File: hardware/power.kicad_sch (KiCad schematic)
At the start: 12 parts, among them Q1 DMG2305UX, U3 TPS61099DRV

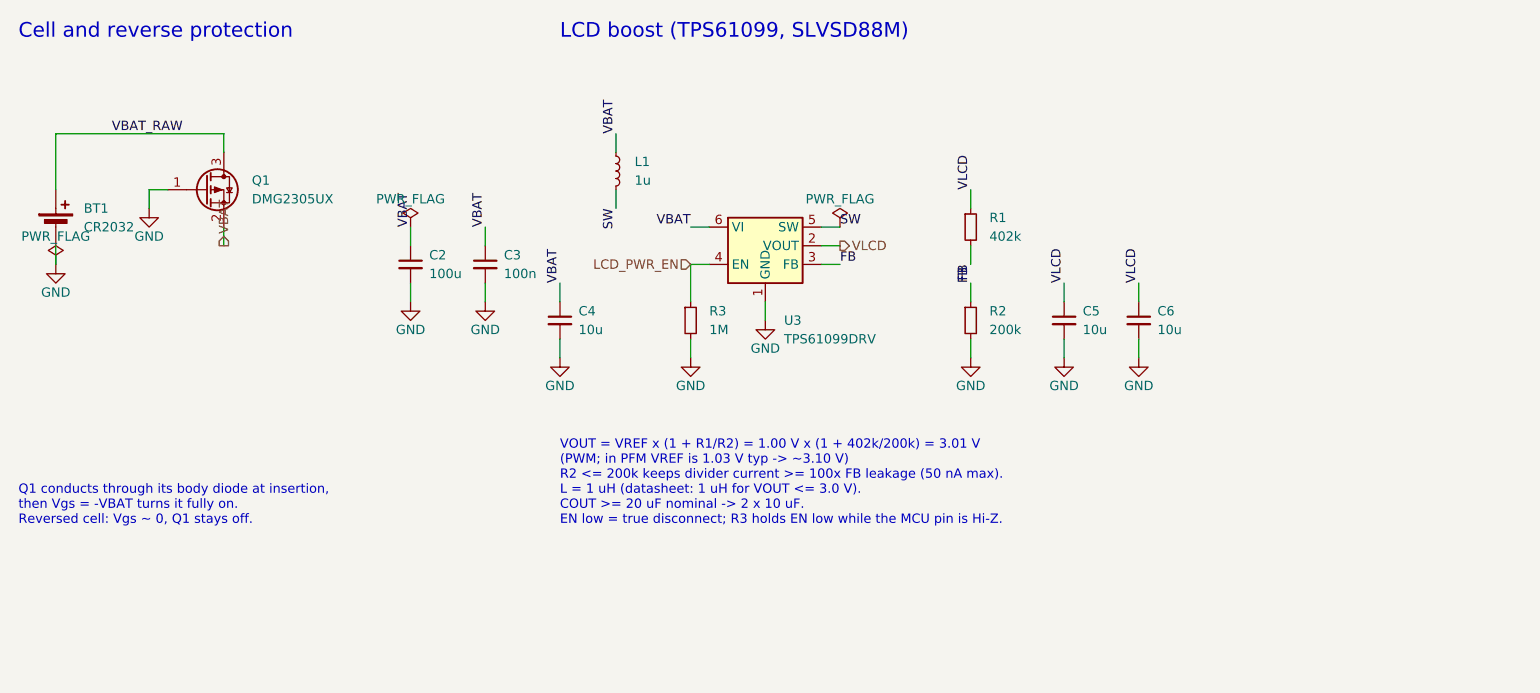
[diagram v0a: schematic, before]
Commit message: Power sheet: add TPS22916C switch ahead of the LCD boost
U5 (TPS22916CYFPR) on LCD_PWR_EN cuts the TPS61099's 0.5-1.6 uA
shutdown current and the 100 uF bulk's leakage off the cell while the
lid is shut. C2 moves to the switched boost input behind R4 (470R),
which limits inrush to ~6.6 mA; the switch's own slew would draw
220-350 mA. R5/C8 (1M/470n) delay the boost EN until C2 has charged.
Always-on VBAT keeps 100 nF + 1 uF.

Adds a project symbol library with the TPS22916C symbol; the footprint
is the TI PicoStar 2x2 0.4 mm land pattern, which matches YFP.
ERC is clean with all severities enabled.

Co-Authored-By: Claude Opus 5.5 (1M context) <noreply@anthropic.com>
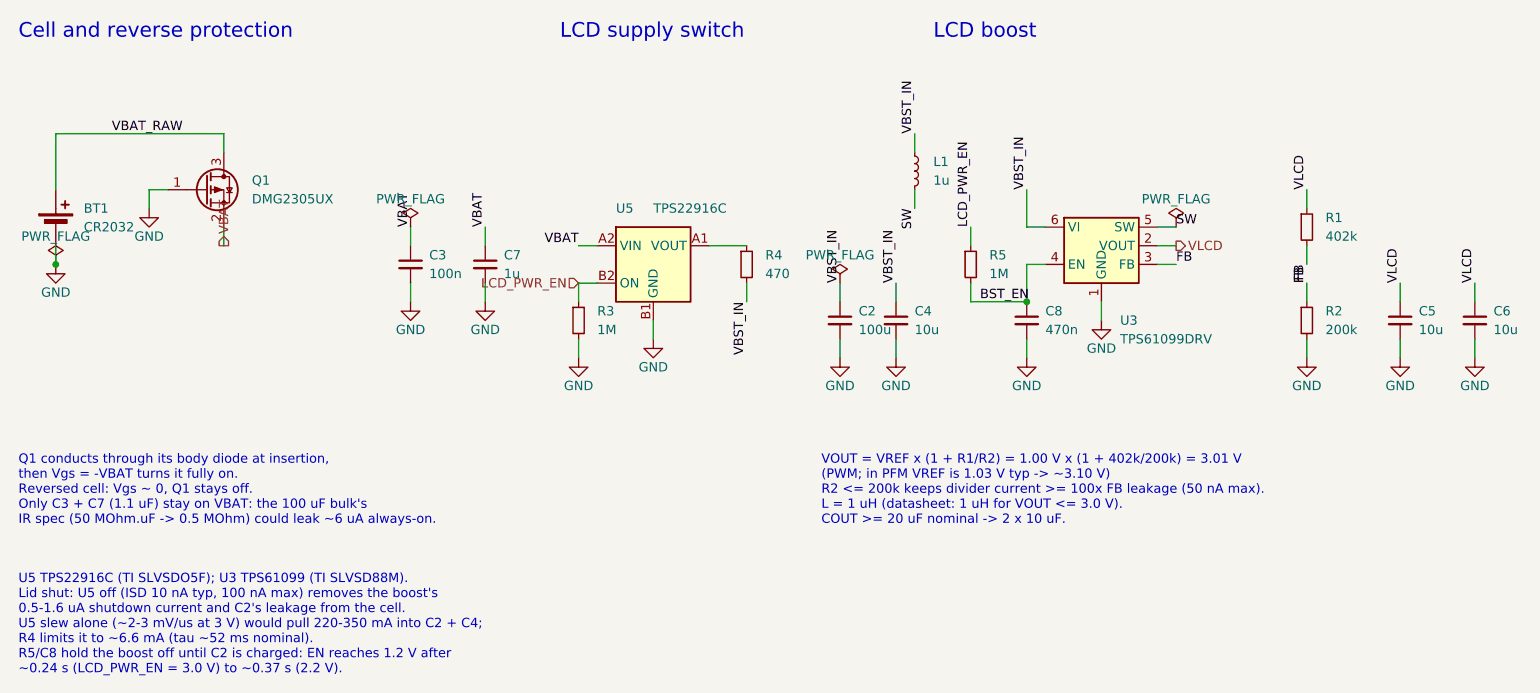
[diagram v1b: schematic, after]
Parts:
- removed Q1: DMG2305UX, Package_TO_SOT_SMD:SOT-23, symbol Transistor_FET:Q_PMOS_GSD
- added C7: 1u, Capacitor_SMD:C_0402_1005Metric, symbol Device:C_Small
- added C8: 470n, Capacitor_SMD:C_0402_1005Metric, symbol Device:C_Small
- added R4: 470, Resistor_SMD:R_0402_1005Metric, symbol Device:R_Small
- added R5: 1M, Resistor_SMD:R_0402_1005Metric, symbol Device:R_Small
- added U3: TPS61099DRV, Package_SON:WSON-6-1EP_2x2mm_P0.65mm_EP1x1.6mm, symbol Regulator_Switching:TPS61099DRV
- added U5: TPS22916C, Package_BGA:Texas_PicoStar_BGA-4_0.758x0.758mm_Layout2x2_P0.4mm, symbol Eigentime32:TPS22916C
- Q1: renamed from U3; value TPS61099DRV -> DMG2305UX; footprint Package_SON:WSON-6-1EP_2x2mm_P0.65mm_EP1x1.6mm -> Package_TO_SOT_SMD:SOT-23; symbol Regulator_Switching:TPS61099DRV -> Transistor_FET:Q_PMOS_GSD; MPN TPS61099DRVR -> DMG2305UX-7; Manufacturer Texas Instruments -> Diodes Incorporated
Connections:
- net FB: now also U3.3 (FB); no longer Q1.3 (FB)
- net GND: now also C7.2, C8.2, U3.1 (GND), U3.7 (GND), U5.B1 (GND); no longer Q1.7 (GND)
- net LCD_PWR_EN: now also R5.1, U5.B2 (ON); no longer Q1.4 (EN)
- net SW: now also U3.5 (SW); no longer Q1.5 (SW)
- net VBAT: now also Q1.2 (S), C7.1, U5.A2 (VIN); no longer C2.1, C4.1, L1.1, Q1.6 (VI)
- net VBAT_RAW: now also Q1.3 (D)
- net VLCD: now also U3.2 (VOUT); no longer Q1.2 (VOUT)
- new net: R4.1, U5.A1 (VOUT)
- new net BST_EN: C8.1, R5.2, U3.4 (EN)
- new net VBST_IN: C2.1, C4.1, L1.1, R4.2, U3.6 (VI)
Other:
- note added: "LCD boost"
- note added: "LCD supply switch"
- note added: "Q1 conducts through its body diode at insertion, then Vgs = -VBAT turns it fully on. Reversed cell: Vgs ~ 0, Q1 stays off. Only C3 + C7 (1.1 uF) stay on VBAT: the 100 uF bulk's IR spec (50 MOhm.uF -> 0.5 MOhm) could leak ~6 uA always-on."
- note added: "U5 TPS22916C (TI SLVSDO5F); U3 TPS61099 (TI SLVSD88M). Lid shut: U5 off (ISD 10 nA typ, 100 nA max) removes the boost's 0.5-1.6 uA shutdown current and C2's leakage from the cell. U5 slew alone (~2-3 mV/us at 3 V) would pull 220-350 mA into C2 + C4; R4 limits it to ~6.6 mA (tau ~52 ms nominal). R5/C8 hold the boost off until C2 is charged: EN reaches 1.2 V after ~0.24 s (LCD_PWR_EN = 3.0 V) to ~0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"
- note added: "VOUT = VREF x (1 + R1/R2) = 1.00 V x (1 + 402k/200k) = 3.01 V (PWM; in PFM VREF is 1.03 V typ -> ~3.10 V) R2 <= 200k keeps divider current >= 100x FB leakage (50 nA max). L = 1 uH (datasheet: 1 uH for VOUT <= 3.0 V). COUT >= 20 uF nominal -> 2 x 10 uF."
- note removed: "LCD boost (TPS61099, SLVSD88M)"
- note removed: "Q1 conducts through its body diode at insertion, then Vgs = -VBAT turns it fully on. Reversed cell: Vgs ~ 0, Q1 stays off."
- note removed: "VOUT = VREF x (1 + R1/R2) = 1.00 V x (1 + 402k/200k) = 3.01 V (PWM; in PFM VREF is 1.03 V typ -> ~3.10 V) R2 <= 200k keeps divider current >= 100x FB leakage (50 nA max). L = 1 uH (datasheet: 1 uH for VOUT <= 3.0 V). COUT >= 20 uF nominal -> 2 x 10 uF. EN low = true disconnect; R3 holds EN low while the MCU pin is Hi-Z."

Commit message: Layout: MCU to 4:30, smaller cell pad, routing rules (unrouted)
Placement reworked for routability: the MCU moves to the widest part
of the ring at ~4:30, with NFC, RTC and lid sensor in the 3 o'clock
strip. The CR2032 negative pad is now 5 mm (project footprint; Keystone
asks for 3.96 mm square minimum) so tracks can run under the cell.

Routing rules are set but the board is not routed yet: 0.127 mm
clearance, 0.2 mm signal and 0.25 mm power tracks (Power netclass),
0.5/0.3 mm vias, 0.2 mm hole-to-copper, and a coil-ring keep-out (no
front tracks or vias between r 16.4 and 19.1 mm).

Freerouting 2.4.1 reaches ~20 of 143 connections unrouted on this
2-layer placement. ERC clean; DRC: 0 violations, 0 parity issues,
143 unrouted.

Co-Authored-By: Claude Opus 5.5 (1M context) <noreply@anthropic.com>
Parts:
- BT1: footprint Battery:BatteryHolder_Keystone_3034_1x20mm -> Eigentime32:BatteryHolder_Keystone_3034_1x20mm_SmallNegPad
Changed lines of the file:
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@@
 		(property "Reference" "BT1" (at 34.29 68.58 0) (effects (font (size 1.27 1.27)) (justify left)))
 		(property "Value" "CR2032" (at 34.29 71.12 0) (effects (font (size 1.27 1.27)) (justify left)))
-		(property "Footprint" "Battery:BatteryHolder_Keystone_3034_1x20mm" (at 30.48 71.12 0) (effects (font (size 1.27 1.27)) (hide yes)))
+		(property "Footprint" "Eigentime32:BatteryHolder_Keystone_3034_1x20mm_SmallNegPad" (at 30.48 71.12 0) (effects (font (size 1.27 1.27)) (hide yes)))
 		(property "Datasheet" "https://www.digikey.com/en/products/detail/keystone-electronics/3034/4499289" (at 30.48 71.12 0) (effects (font (size 1.27 1.27)) (hide yes)))
 		(property "Description" "CR2032 SMT retainer, 4.06 mm above board" (at 30.48 71.12 0) (effects (font (size 1.27 1.27)) (hide yes)))
